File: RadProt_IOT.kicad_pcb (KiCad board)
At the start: 2 copper layers, 80 x 80 mm, 10 parts, among them SW1 Config, U1 RaspberryPi_Pico_W

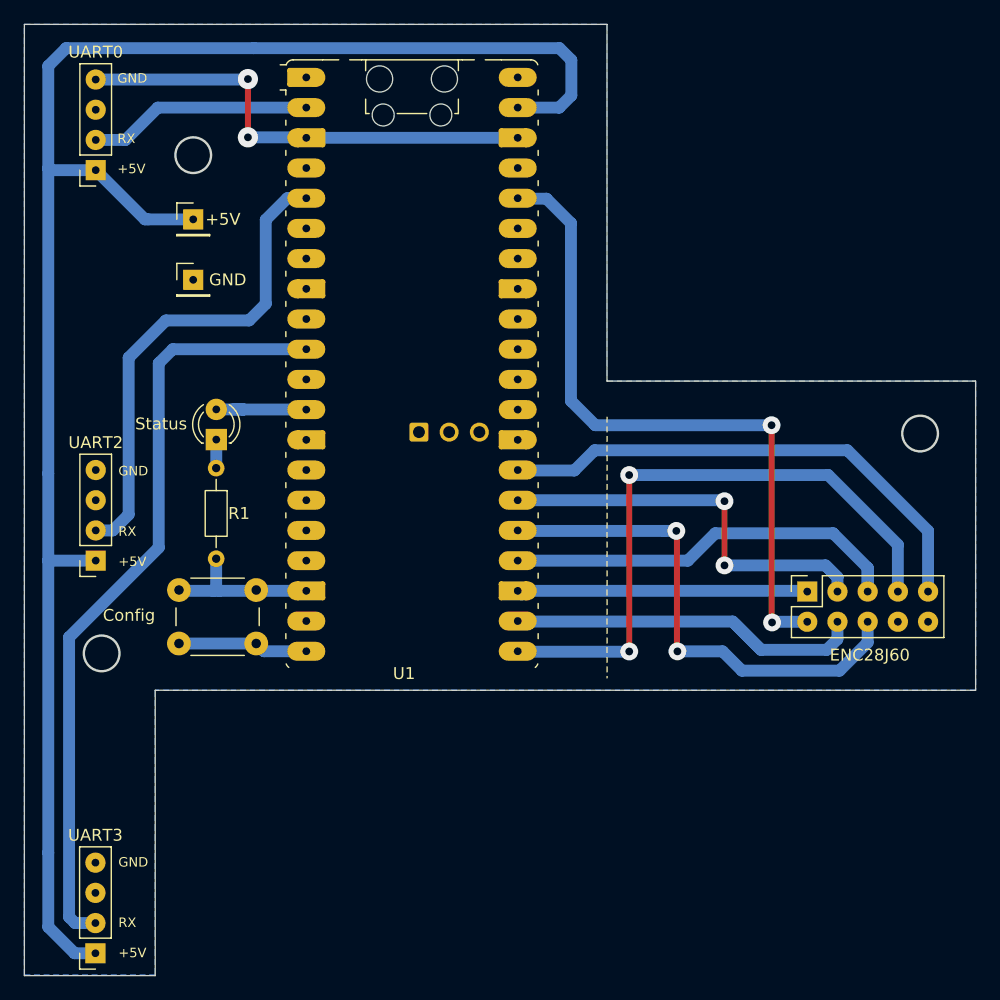
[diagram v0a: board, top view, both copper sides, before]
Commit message: added Power Ledd
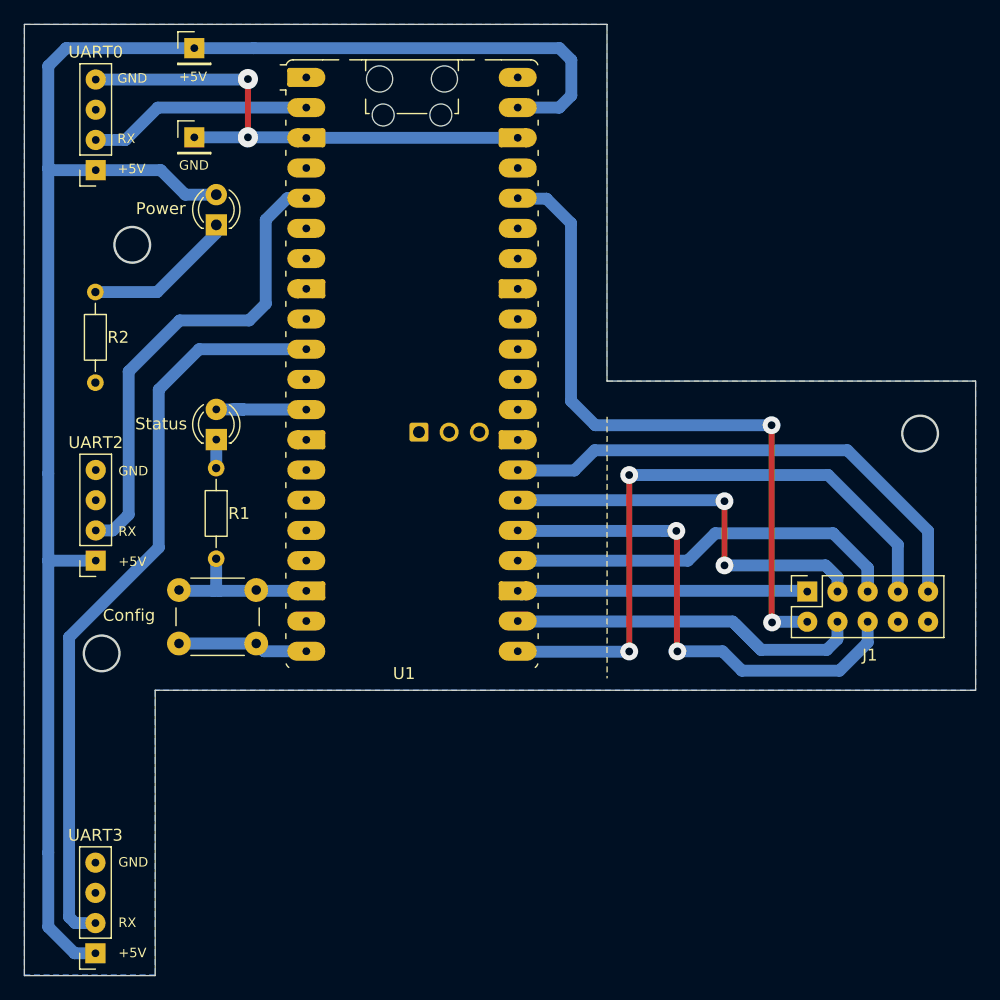
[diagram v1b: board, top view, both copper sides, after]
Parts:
- added D2: Power, LED_THT:LED_D3.0mm, F.Cu at (117.1, 95.9)
- added R2: 330, Resistor_THT:R_Axial_DIN0204_L3.6mm_D1.6mm_P7.62mm_Horizontal, F.Cu at (107.0, 101.5)
- moved J5 14.4 mm to (115.3, 81.0)
- moved J6 12.0 mm to (115.3, 88.5)
- renumbered ENC28J60 to J1, +5V to J5, GND to J6
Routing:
- net Net-(D2-K): track 0.00 -> 12.9 mm
- net GND: track 78.7 -> 83.2 mm
- net /UART3_RX: track 65.0 -> 63.7 mm
- net +5V: track 148.2 -> 149.3 mm
- net /UART2_RX: track 41.3 -> 40.6 mm
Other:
- outline, holes or cut-outs redrawn

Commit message: changed some labels
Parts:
- moved J5 32.9 mm to (148.0, 84.6)
- moved J6 32.7 mm to (148.0, 89.8)
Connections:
- D2 pad 2: +5V -> Net-(D2-A)
- J1 pad VCC: Net-(U1-3V3) -> Net-(D2-A)
- U1 pad 36: Net-(U1-3V3) -> Net-(D2-A)
- UART0 pad 1: +5V -> Net-(D2-A)
- UART2 pad 1: +5V -> Net-(D2-A)
- UART3 pad 1: +5V -> Net-(D2-A)
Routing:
- net Net-(D2-A): track 0.00 -> 204.3 mm, vias 0 -> 2
- net +5V: track 149.3 -> 6.04 mm
- net Net-(U1-3V3): track 57.0 -> 0.00 mm, vias 2 -> 0
- net GND: track 83.2 -> 67.0 mm
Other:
- board text added: "Enc28j60"
- board text added: "Raspberry Pi Pico W"

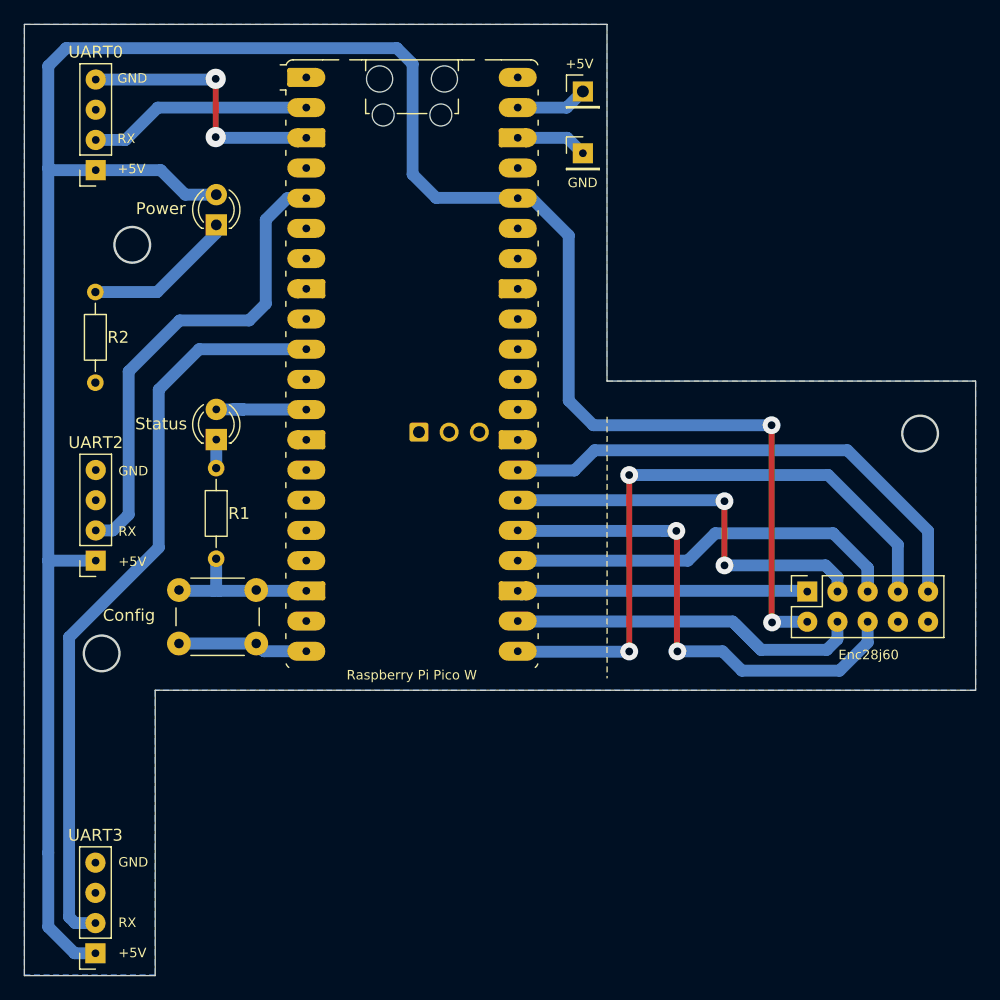
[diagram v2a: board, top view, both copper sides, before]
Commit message: added logo and changed hole sizes from 0.65 to 0.8
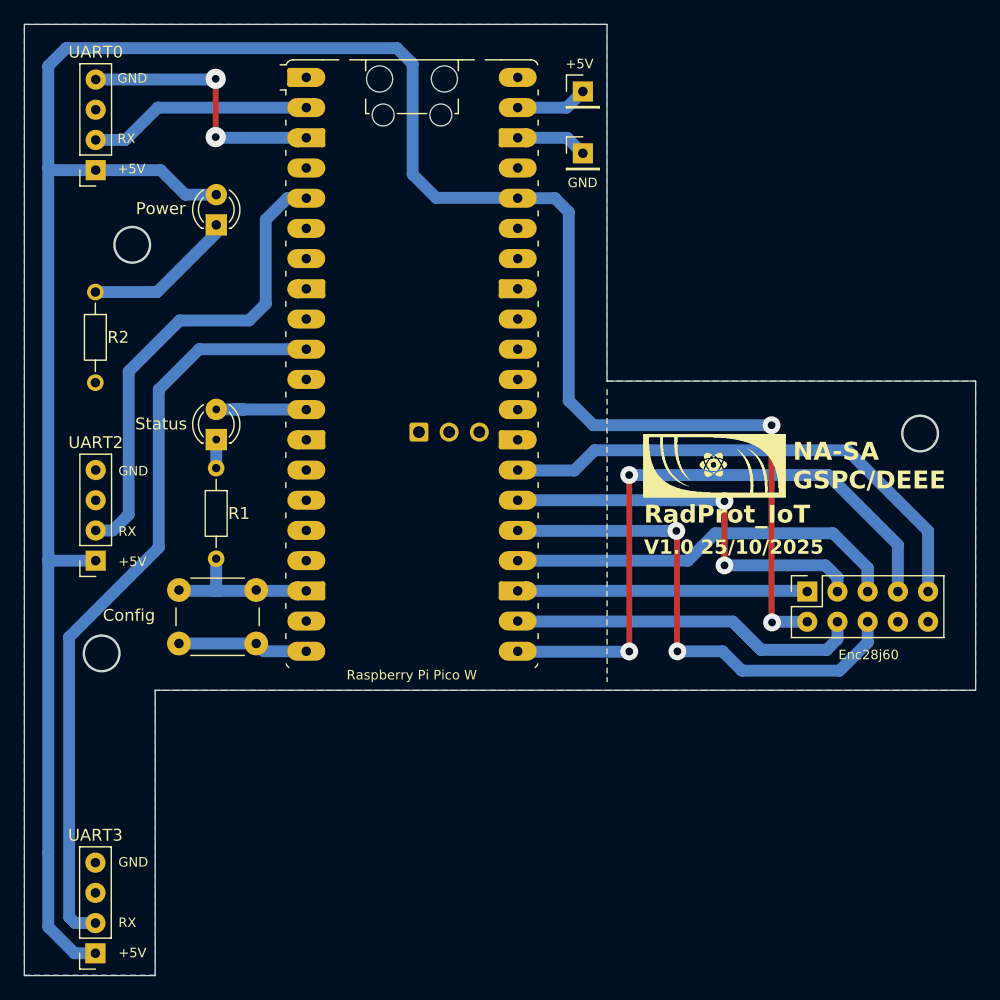
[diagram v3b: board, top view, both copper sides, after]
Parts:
- added LOGO: , Nasa:logo_nasa, F.Cu at (153.0, 113.5)
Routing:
- net Net-(D2-A): track 204.3 -> 205.4 mm
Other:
- board text added: "NA-SA GSPC/DEEE"
- board text added: "RadProt_IoT"
- board text added: "V1.0 25/10/2025"
